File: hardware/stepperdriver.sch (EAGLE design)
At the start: 42 parts, among them IC1 L297, IC2 L298, X2 1751248, X3 1751264

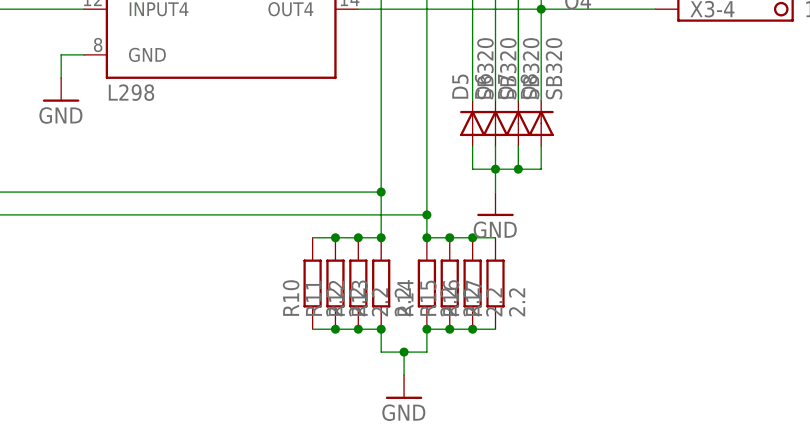
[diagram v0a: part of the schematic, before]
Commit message: Shuntwiderstände auf 2 Stück reduziert
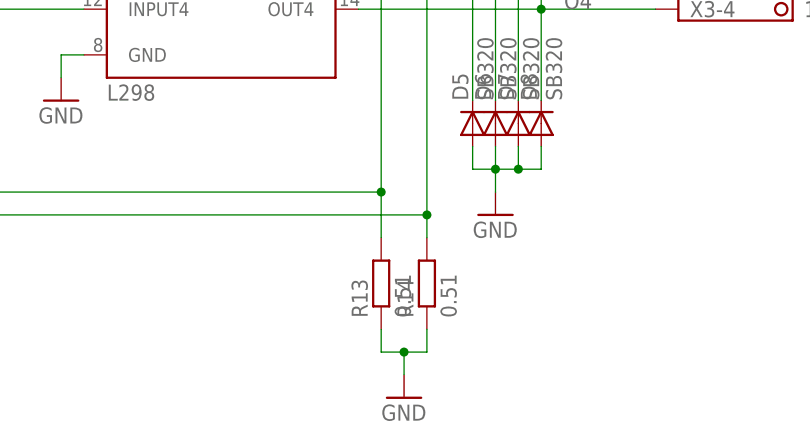
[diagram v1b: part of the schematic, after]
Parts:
- removed R10, R11, R12, R15, R16, R17: 2.2, resistor:R-EU_0411/15
- R13, R14: value 2.2 -> 0.51
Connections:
- net GND: no longer R10.1, R11.1, R12.1, R15.1, R16.1, R17.1
- net N$11: no longer R15.2, R16.2, R17.2
- net N$9: no longer R10.2, R11.2, R12.2
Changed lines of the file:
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@@
 <part name="C3" library="resistor" deviceset="C-EU" device="050-035X075" value="3.3n"/>
 <part name="GND14" library="supply1" deviceset="GND" device=""/>
-<part name="R10" library="resistor" deviceset="R-EU_" device="0411/15" value="2.2"/>
-<part name="R11" library="resistor" deviceset="R-EU_" device="0411/15" value="2.2"/>
-<part name="R12" library="resistor" deviceset="R-EU_" device="0411/15" value="2.2"/>
-<part name="R13" library="resistor" deviceset="R-EU_" device="0411/15" value="2.2"/>
-<part name="R14" library="resistor" deviceset="R-EU_" device="0411/15" value="2.2"/>
-<part name="R15" library="resistor" deviceset="R-EU_" device="0411/15" value="2.2"/>
-<part name="R16" library="resistor" deviceset="R-EU_" device="0411/15" value="2.2"/>
-<part name="R17" library="resistor" deviceset="R-EU_" device="0411/15" value="2.2"/>
+<part name="R13" library="resistor" deviceset="R-EU_" device="0411/15" value="0.51"/>
+<part name="R14" library="resistor" deviceset="R-EU_" device="0411/15" value="0.51"/>
 <part name="GND15" library="supply1" deviceset="GND" device=""/>
 <part name="GND16" library="supply1" deviceset="GND" device=""/>
@@
 <instance part="C3" gate="G$1" x="99.06" y="81.28"/>
 <instance part="GND14" gate="1" x="99.06" y="71.12"/>
-<instance part="R10" gate="G$1" x="152.4" y="30.48" rot="R90"/>
-<instance part="R11" gate="G$1" x="154.94" y="30.48" rot="R90"/>
-<instance part="R12" gate="G$1" x="157.48" y="30.48" rot="R90"/>
 <instance part="R13" gate="G$1" x="160.02" y="30.48" rot="R90"/>
 <instance part="R14" gate="G$1" x="165.1" y="30.48" rot="R90"/>
-<instance part="R15" gate="G$1" x="167.64" y="30.48" rot="R90"/>
-<instance part="R16" gate="G$1" x="170.18" y="30.48" rot="R90"/>
-<instance part="R17" gate="G$1" x="172.72" y="30.48" rot="R90"/>
 <instance part="GND15" gate="1" x="35.56" y="154.94"/>
 <instance part="GND16" gate="1" x="55.88" y="154.94"/>
@@
 <wire x1="162.56" y1="22.86" x2="162.56" y2="20.32" width="0.1524" layer="91"/>
 <junction x="162.56" y="22.86"/>
-<pinref part="R10" gate="G$1" pin="1"/>
-<pinref part="R11" gate="G$1" pin="1"/>
-<wire x1="152.4" y1="25.4" x2="154.94" y2="25.4" width="0.1524" layer="91"/>
-<pinref part="R12" gate="G$1" pin="1"/>
-<wire x1="154.94" y1="25.4" x2="157.48" y2="25.4" width="0.1524" layer="91"/>
-<junction x="154.94" y="25.4"/>
 <pinref part="R13" gate="G$1" pin="1"/>
-<wire x1="157.48" y1="25.4" x2="160.02" y2="25.4" width="0.1524" layer="91"/>
-<junction x="157.48" y="25.4"/>
 <wire x1="160.02" y1="25.4" x2="160.02" y2="22.86" width="0.1524" layer="91"/>
-<junction x="160.02" y="25.4"/>
 <pinref part="R14" gate="G$1" pin="1"/>
 <wire x1="165.1" y1="22.86" x2="165.1" y2="25.4" width="0.1524" layer="91"/>
-<pinref part="R15" gate="G$1" pin="1"/>
-<wire x1="165.1" y1="25.4" x2="167.64" y2="25.4" width="0.1524" layer="91"/>
-<junction x="165.1" y="25.4"/>
-<pinref part="R16" gate="G$1" pin="1"/>
-<wire x1="167.64" y1="25.4" x2="170.18" y2="25.4" width="0.1524" layer="91"/>
-<junction x="167.64" y="25.4"/>
-<pinref part="R17" gate="G$1" pin="1"/>
-<wire x1="170.18" y1="25.4" x2="172.72" y2="25.4" width="0.1524" layer="91"/>
-<junction x="170.18" y="25.4"/>
 </segment>
 <segment>
@@
 <net name="N$9" class="2">
 <segment>
-<pinref part="R10" gate="G$1" pin="2"/>
-<pinref part="R11" gate="G$1" pin="2"/>
-<wire x1="152.4" y1="35.56" x2="154.94" y2="35.56" width="0.1524" layer="91"/>
-<pinref part="R12" gate="G$1" pin="2"/>
-<wire x1="154.94" y1="35.56" x2="157.48" y2="35.56" width="0.1524" layer="91"/>
-<junction x="154.94" y="35.56"/>
 <pinref part="R13" gate="G$1" pin="2"/>
-<wire x1="157.48" y1="35.56" x2="160.02" y2="35.56" width="0.1524" layer="91"/>
-<junction x="157.48" y="35.56"/>
 <pinref part="IC2" gate="L298" pin="SEN_B"/>
 <wire x1="157.48" y1="73.66" x2="160.02" y2="73.66" width="0.1524" layer="91"/>
@@
 <wire x1="38.1" y1="40.64" x2="160.02" y2="40.64" width="0.1524" layer="91"/>
 <wire x1="160.02" y1="35.56" x2="160.02" y2="40.64" width="0.1524" layer="91"/>
-<junction x="160.02" y="35.56"/>
 <junction x="160.02" y="40.64"/>
 </segment>
@@
 <net name="N$11" class="2">
 <segment>
-<pinref part="R17" gate="G$1" pin="2"/>
-<pinref part="R16" gate="G$1" pin="2"/>
-<wire x1="172.72" y1="35.56" x2="170.18" y2="35.56" width="0.1524" layer="91"/>
-<pinref part="R15" gate="G$1" pin="2"/>
-<wire x1="170.18" y1="35.56" x2="167.64" y2="35.56" width="0.1524" layer="91"/>
-<junction x="170.18" y="35.56"/>
 <pinref part="R14" gate="G$1" pin="2"/>
-<wire x1="167.64" y1="35.56" x2="165.1" y2="35.56" width="0.1524" layer="91"/>
-<junction x="167.64" y="35.56"/>
 <pinref part="IC2" gate="L298" pin="SEN_A"/>
 <wire x1="157.48" y1="76.2" x2="165.1" y2="76.2" width="0.1524" layer="91"/>
@@
 <wire x1="33.02" y1="38.1" x2="165.1" y2="38.1" width="0.1524" layer="91"/>
 <wire x1="165.1" y1="35.56" x2="165.1" y2="38.1" width="0.1524" layer="91"/>
-<junction x="165.1" y="35.56"/>
 <junction x="165.1" y="38.1"/>
 </segment>
